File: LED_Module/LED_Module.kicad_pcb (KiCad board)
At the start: 2 copper layers, 46 parts, among them J1 Conn_02x05_Odd_Even, J2 Conn_01x03_Male, J3 ESP8266 Header, J4 Barrel_Jack, SW1 SW_Push, SW2 SW_Push, U1 LD1117S33TR_SOT223, U2 STM32F091RCTx, U3 TPS62A02DRL, U4 24AA32AF EEPROM

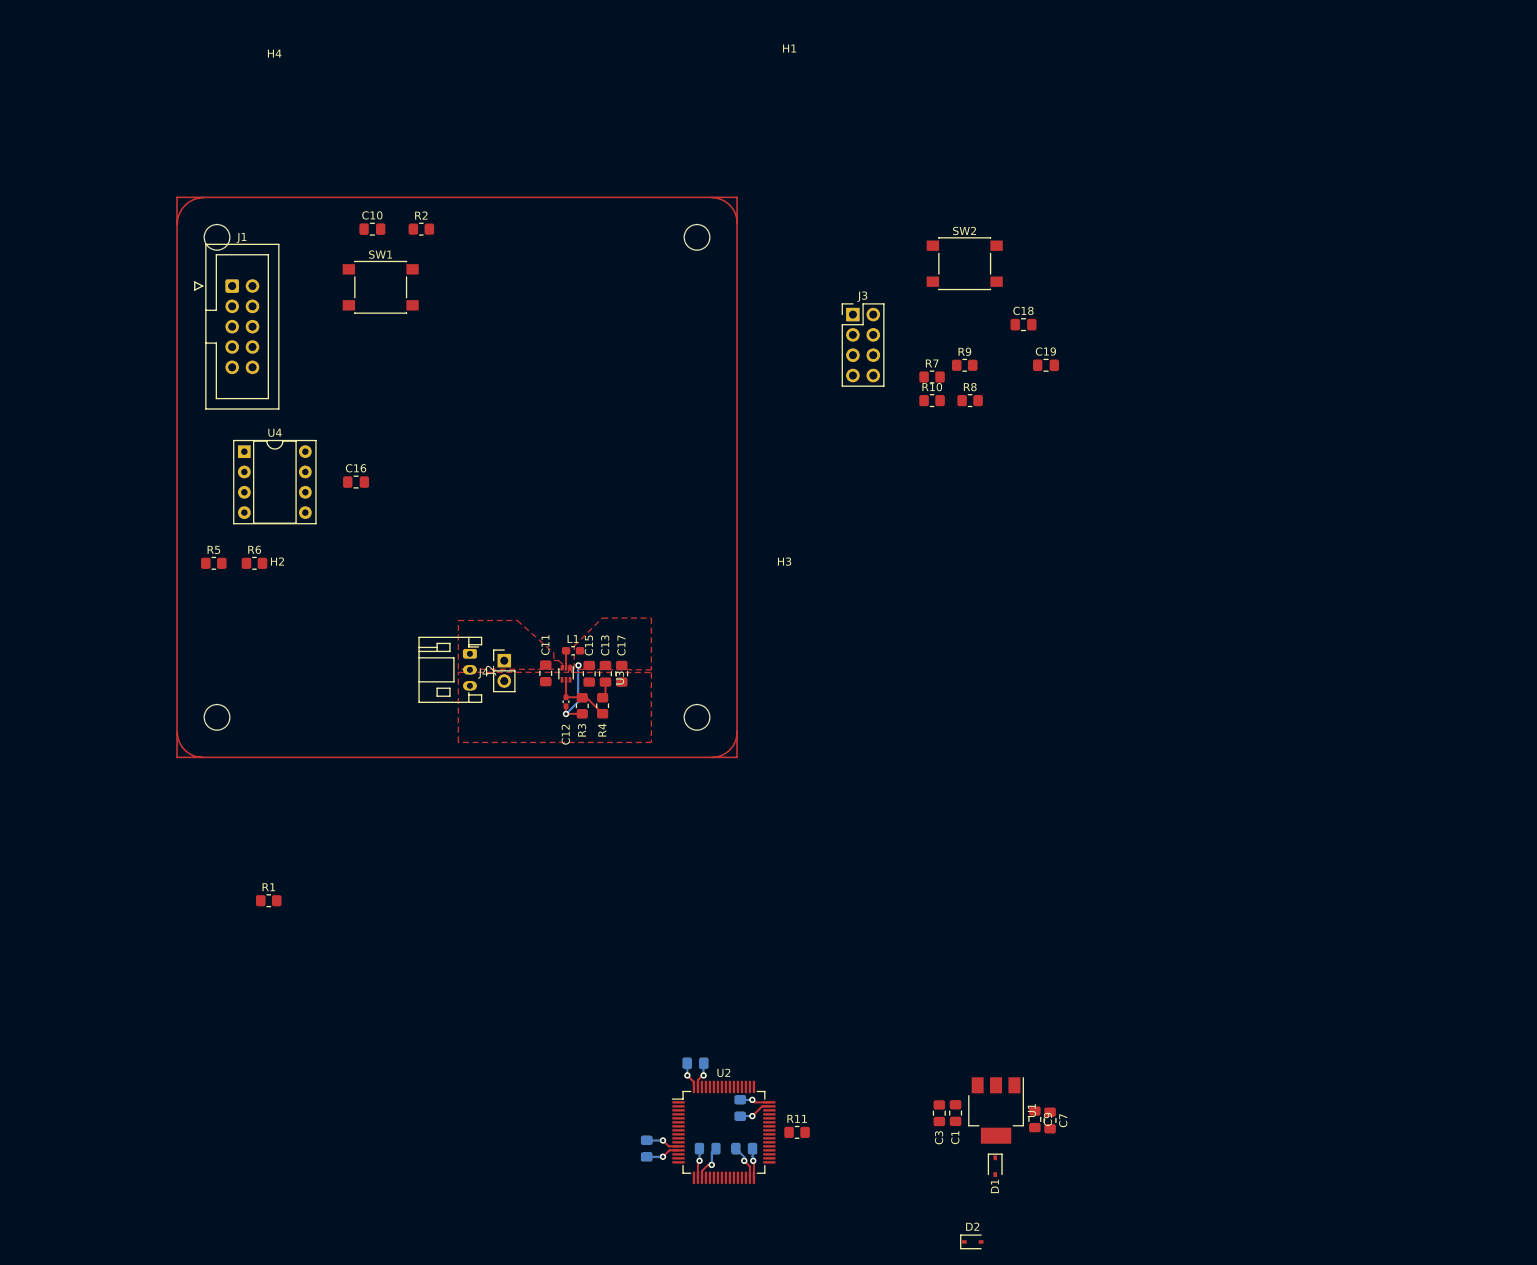
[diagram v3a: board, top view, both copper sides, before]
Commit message: Systems laid out and 3.3V connected
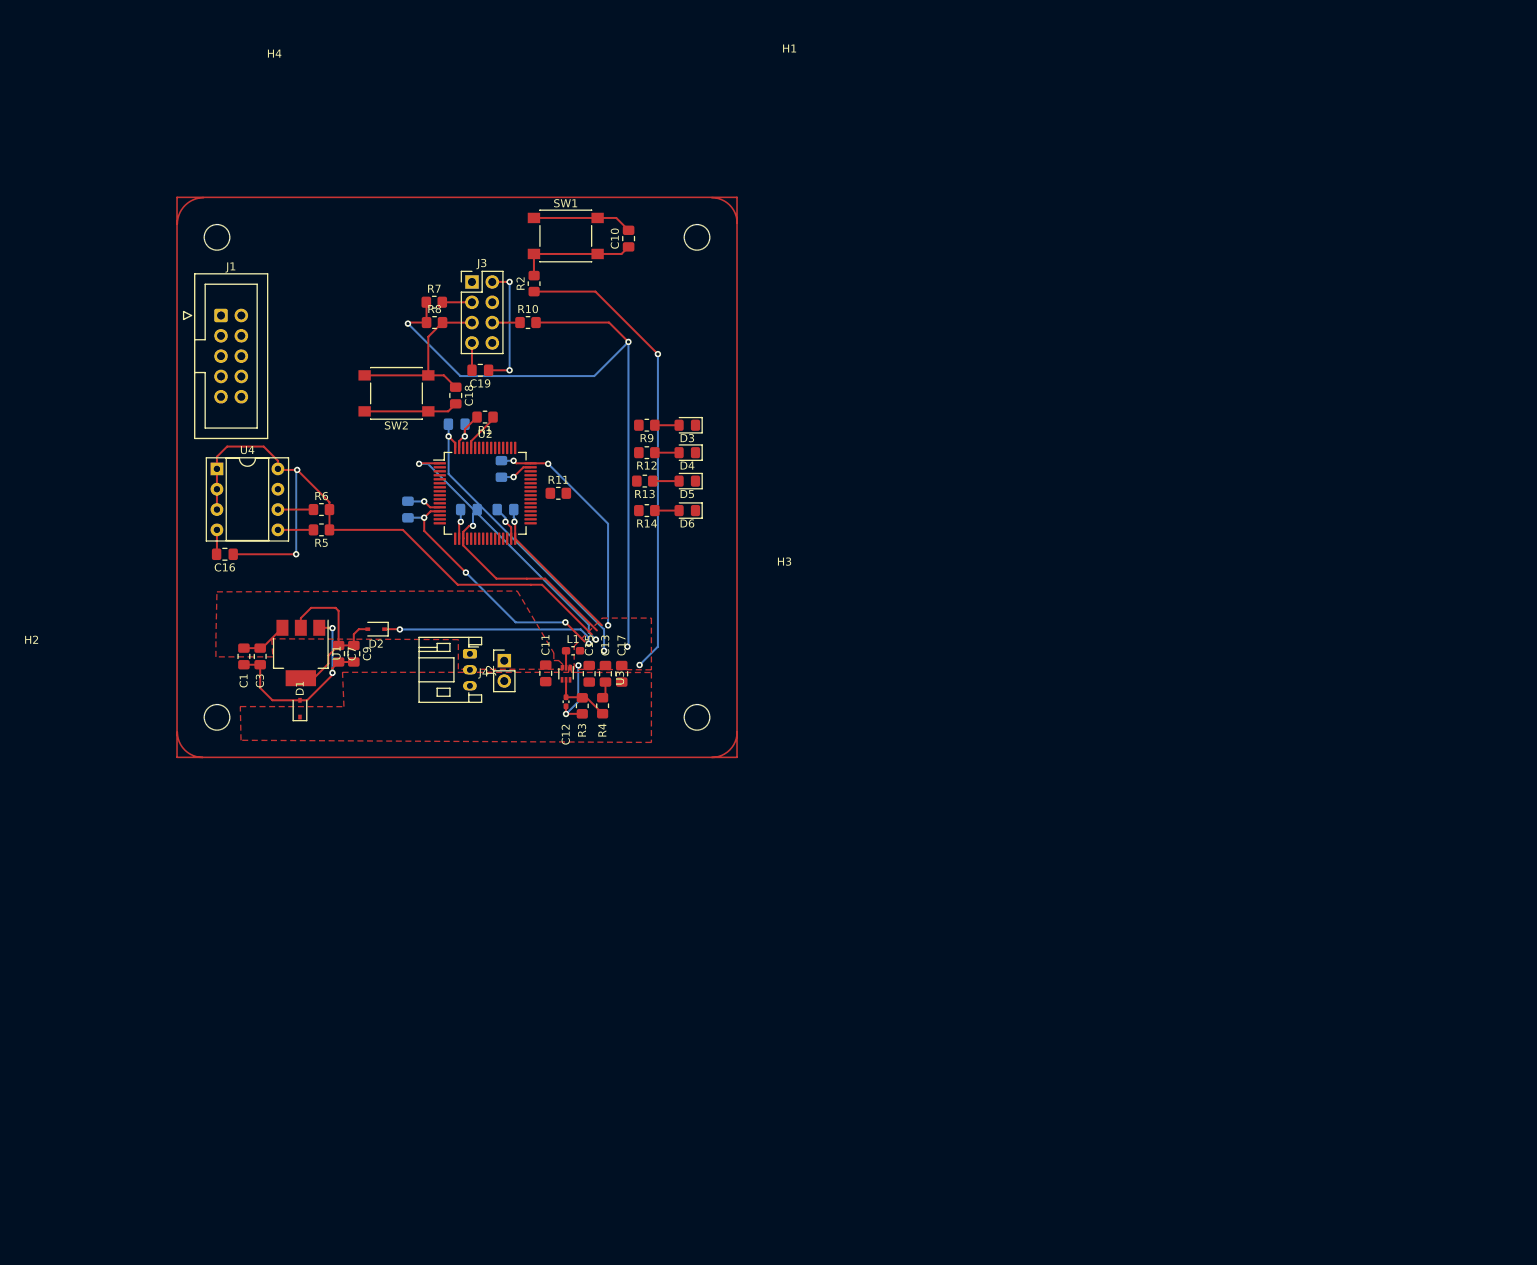
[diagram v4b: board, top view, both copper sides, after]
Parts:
- added D3: LED, LED_SMD:LED_0805_2012Metric_Pad1.15x1.40mm_HandSolder, F.Cu at (113.8, 78.5)
- added D4: LED, LED_SMD:LED_0805_2012Metric_Pad1.15x1.40mm_HandSolder, F.Cu at (113.8, 81.9)
- added D5: LED, LED_SMD:LED_0805_2012Metric_Pad1.15x1.40mm_HandSolder, F.Cu at (113.8, 85.5)
- added D6: LED, LED_SMD:LED_0805_2012Metric_Pad1.15x1.40mm_HandSolder, F.Cu at (113.8, 89.2)
- added R12: 3K, Resistor_SMD:R_0805_2012Metric_Pad1.20x1.40mm_HandSolder, F.Cu at (108.7, 81.9)
- added R13: 3K, Resistor_SMD:R_0805_2012Metric_Pad1.20x1.40mm_HandSolder, F.Cu at (108.5, 85.5)
- added R14: 3K, Resistor_SMD:R_0805_2012Metric_Pad1.20x1.40mm_HandSolder, F.Cu at (108.7, 89.2)
- R9: value R -> 3K
- moved D2 106.9 mm to (74.9, 104.0), turned to 180 degrees
- moved C7 106.4 mm to (70.2, 107.0)
- moved C1 105.7 mm to (58.4, 107.4)
- moved D1 104.0 mm to (65.4, 113.9), turned to 90 degrees
- moved U1 104.0 mm to (65.5, 107.0)
- moved C9 103.1 mm to (72.1, 107.0)
- moved C3 102.3 mm to (60.4, 107.4)
- moved C2 85.3 mm to (86.5, 89.0)
- moved C4 85.3 mm to (85.0, 78.4)
- moved C5 85.3 mm to (91.1, 89.0)
- moved C8 85.3 mm to (78.9, 89.0)
- moved C6 85.3 mm to (90.6, 83.9)
- moved R11 85.3 mm to (97.7, 87.0)
- moved U2 85.3 mm to (88.5, 87.0)
- moved SW2 72.9 mm to (77.4, 74.5), turned to 180 degrees
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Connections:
- D1 pad 1: GND -> BUCK_GND
- J3 pad 2: /CH_PD -> GND
- J3 pad 3: /RST -> /CH_PD
- J3 pad 4: 3.3V -> unconnected-(J3-Pad4)
- J3 pad 5: /PC12 -> /RST
- J3 pad 7: /GPIO2 -> 3.3V
- J3 pad 8: GND -> /PC12
- R9 pad 1: /GPIO2 -> Net-(D3-Pad2)
- R9 pad 2: GND -> /PC6
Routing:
- net 3.3V: track 29.5 -> 450.1 mm, vias 7 -> 23
- net GND: track 19.9 -> 66.1 mm, vias 5 -> 7
- net Net-(C1-Pad2): track 0.00 -> 27.1 mm, vias 0 -> 2
- net Net-(C7-Pad1): track 0.00 -> 23.3 mm
- net /RST: track 0.00 -> 23.0 mm
- net /NRST: track 0.00 -> 14.9 mm
- net 5V: track 0.06 -> 5.93 mm
- net /BOOT0: track 0.00 -> 4.98 mm
- net /EEPROM_SDA: track 0.00 -> 4.45 mm
- net /EEPROM_SCL: track 0.00 -> 4.45 mm
- net /CH_PD: track 0.00 -> 3.71 mm
- net /GPIO0: track 0.00 -> 3.47 mm
- net Net-(D5-Pad2): track 0.00 -> 3.28 mm
- net Net-(D6-Pad2): track 0.00 -> 3.03 mm
- net Net-(D4-Pad2): track 0.00 -> 3.03 mm
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
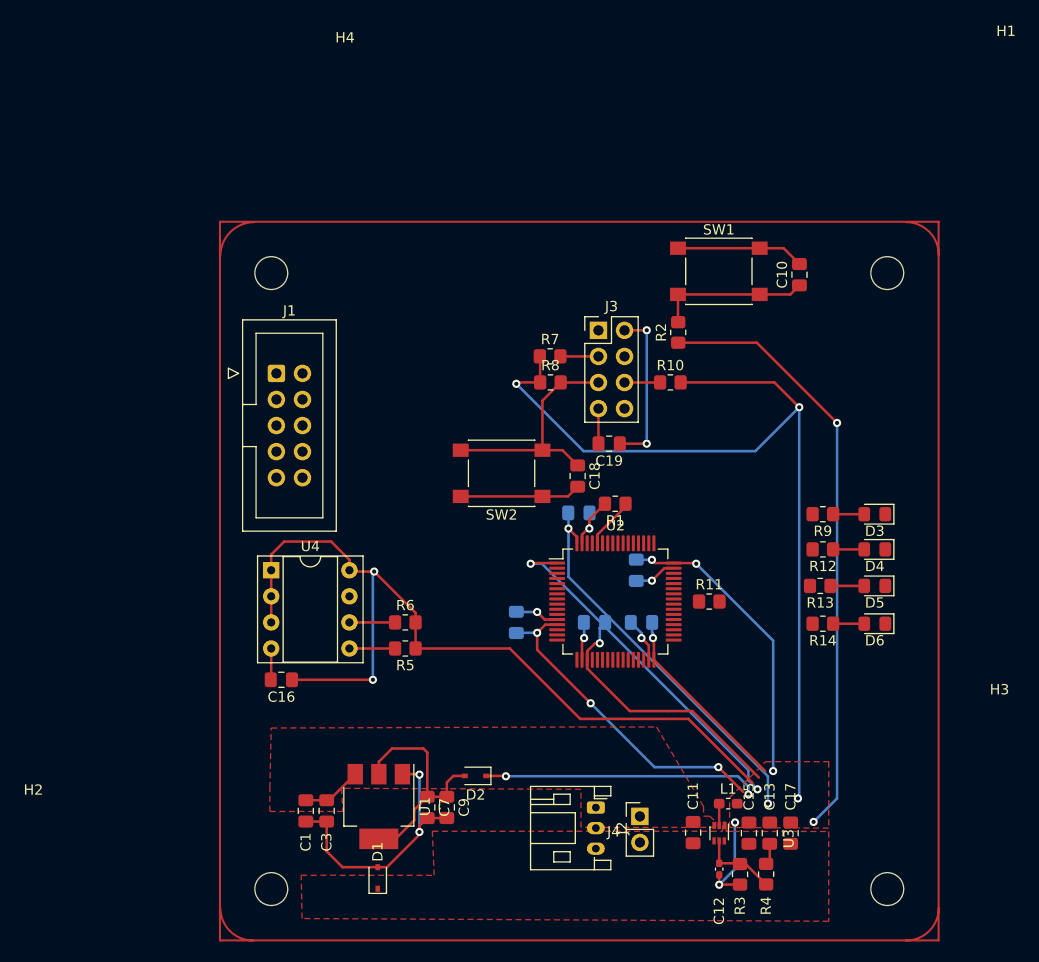
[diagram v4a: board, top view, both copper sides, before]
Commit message: Power and ground planes plus complete routing
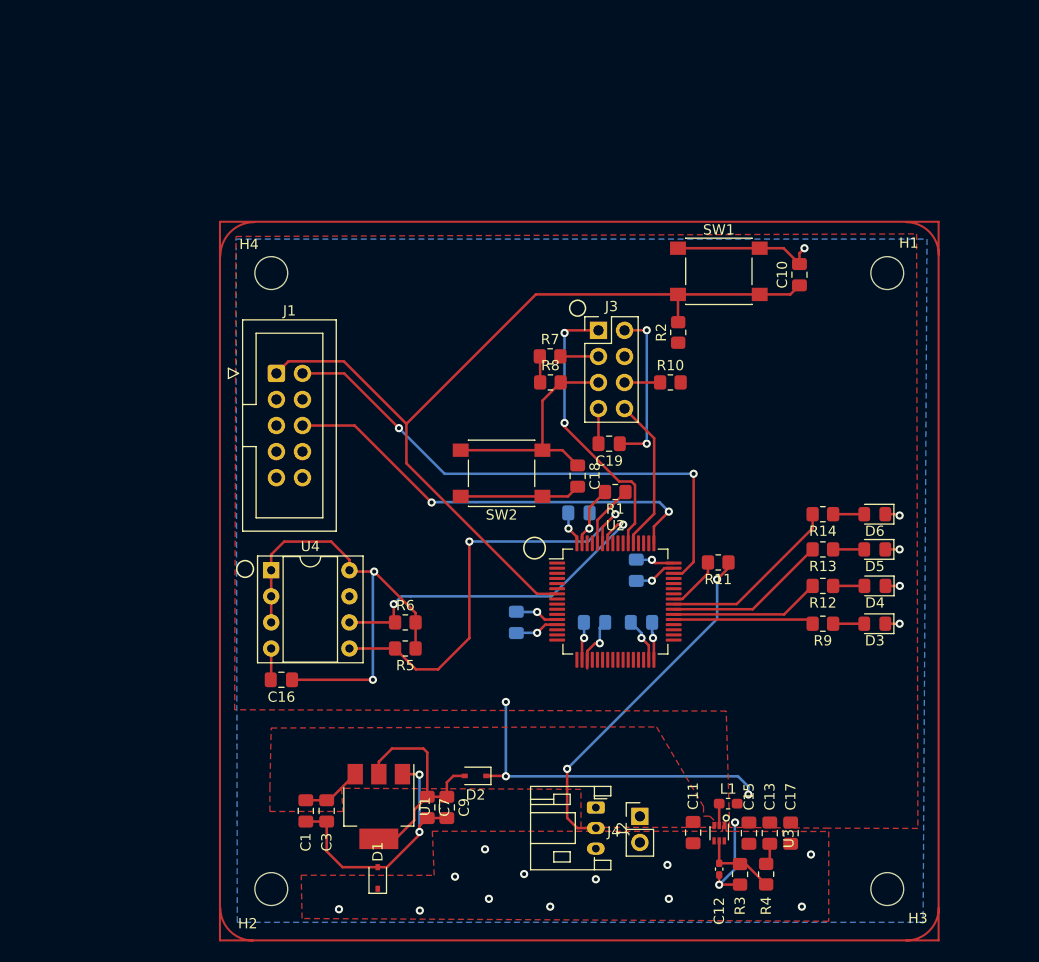
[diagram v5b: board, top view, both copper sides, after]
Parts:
- moved D3 10.7 mm to (113.8, 89.2)
- moved D6 10.7 mm to (113.8, 78.5)
- moved R14 10.7 mm to (108.7, 78.5)
- moved R9 10.7 mm to (108.7, 89.2)
- moved R11 3.91 mm to (98.5, 83.2), turned to 180 degrees
- moved R13 3.57 mm to (108.7, 81.9)
- moved D4 3.56 mm to (113.8, 85.5)
- moved D5 3.56 mm to (113.8, 81.9)
- moved R12 3.56 mm to (108.7, 85.5)
- moved R1 1.14 mm to (88.5, 76.3)
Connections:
- C10 pad 2: GND -> BUCK_GND
- C16 pad 2: GND -> BUCK_GND
- C18 pad 2: GND -> BUCK_GND
- C19 pad 1: GND -> BUCK_GND
- C2 pad 2: GND -> BUCK_GND
- C4 pad 2: GND -> BUCK_GND
- C5 pad 2: GND -> BUCK_GND
- C6 pad 2: GND -> BUCK_GND
- C8 pad 2: GND -> BUCK_GND
- D3 pad 1: GND -> BUCK_GND
- D4 pad 1: GND -> BUCK_GND
- D5 pad 1: GND -> BUCK_GND
- D6 pad 1: GND -> BUCK_GND
- J1 pad 3: GND -> BUCK_GND
- J1 pad 4: GND -> BUCK_GND
- J3 pad 2: GND -> BUCK_GND
- R1 pad 2: GND -> BUCK_GND
- SW1 pad 1: GND -> BUCK_GND
- SW2 pad 1: GND -> BUCK_GND
- U2 pad 12: GND -> BUCK_GND
- U2 pad 18: GND -> BUCK_GND
- U2 pad 31: GND -> BUCK_GND
- U2 pad 47: GND -> BUCK_GND
- U2 pad 63: GND -> BUCK_GND
- U4 pad 4: GND -> BUCK_GND
- U4 pad 7: GND -> BUCK_GND
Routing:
- net 3.3V: track 450.1 -> 116.9 mm, vias 23 -> 12
- net BUCK_GND: track 2.10 -> 76.7 mm, vias 0 -> 24
- net /NRST: track 14.9 -> 86.1 mm
- net GND: track 66.1 -> 0.00 mm, vias 7 -> 0
- net /PA13: track 0.00 -> 53.1 mm, vias 0 -> 2
- net /PA14: track 0.00 -> 42.9 mm, vias 0 -> 2
- net /EEPROM_SDA: track 4.45 -> 41.9 mm, vias 0 -> 2
- net Net-(J2-Pad2): track 0.00 -> 34.6 mm, vias 0 -> 2
- net /EEPROM_SCL: track 4.45 -> 34.6 mm, vias 0 -> 2
- net /PD2: track 0.00 -> 27.7 mm, vias 0 -> 2
- net /PC9: track 0.00 -> 18.0 mm
- net /PC8: track 0.00 -> 15.9 mm
- net /PC12: track 0.00 -> 15.2 mm
- net /PC7: track 0.00 -> 14.7 mm
- net /PC6: track 0.00 -> 13.7 mm
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- added copper zone on B.Cu, net BUCK_GND

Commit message: Added bulk capacitor, diode, and some extra vias
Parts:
- added C14: 100uF, Capacitor_THT:C_Rect_L7.0mm_W2.0mm_P5.00mm, F.Cu at (89.9, 111.6)
- added D7: BAT60JFILM, Diode_SMD:D_SOD-323, F.Cu at (109.6, 106.0)
- moved J4 2.18 mm to (93.1, 108.0)
- moved L1 0.39 mm to (99.6, 107.1)
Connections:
- C12 pad 1: 3.3V -> BUCK_3.3V
- C13 pad 1: 3.3V -> BUCK_3.3V
- C15 pad 1: 3.3V -> BUCK_3.3V
- C17 pad 1: 3.3V -> BUCK_3.3V
- L1 pad 2: 3.3V -> BUCK_3.3V
- R3 pad 1: 3.3V -> BUCK_3.3V
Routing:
- net 3.3V: track 116.9 -> 82.3 mm, vias 12 -> 9
- net BUCK_3.3V: track 0.00 -> 9.71 mm, vias 0 -> 2
- net BUCK_GND: track 76.7 -> 85.0 mm, vias 24 -> 25
- net /PB11: track 0.00 -> 4.50 mm, vias 0 -> 1
- net /PB14: track 0.00 -> 4.24 mm, vias 0 -> 1
- net /PB10: track 0.00 -> 3.70 mm, vias 0 -> 1
- net /PB13: track 0.00 -> 3.64 mm, vias 0 -> 1
- net /PA3: track 0.00 -> 3.55 mm, vias 0 -> 1
- net /PA6: track 0.00 -> 3.10 mm, vias 0 -> 1
- net /PA5: track 0.00 -> 2.94 mm, vias 0 -> 1
- net /PA2: track 0.00 -> 2.36 mm, vias 0 -> 1
- net Net-(L1-Pad1): track 1.93 -> 0.00 mm
- added copper zone on F.Cu, net BUCK_3.3V

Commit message: PCB design updated for week 8 design review
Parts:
- added D8: LED, LED_SMD:LED_0805_2012Metric_Pad1.15x1.40mm_HandSolder, F.Cu at (57.5, 101.0)
- added D9: LED, LED_SMD:LED_0805_2012Metric_Pad1.15x1.40mm_HandSolder, F.Cu at (116.6, 101.6)
- added R15: 3K, Resistor_SMD:R_0805_2012Metric_Pad1.20x1.40mm_HandSolder, F.Cu at (62.2, 100.8)
- added R16: 3K, Resistor_SMD:R_0805_2012Metric_Pad1.20x1.40mm_HandSolder, F.Cu at (116.6, 106.4)
- C13, C15, C17: footprint Capacitor_SMD:C_0805_2012Metric_Pad1.18x1.45mm_HandSolder -> Capacitor_SMD:C_1206_3216Metric_Pad1.33x1.80mm_HandSolder
- moved C17 1.66 mm to (107.2, 109.1)
- moved C13 1.41 mm to (104.9, 109.1)
- moved C15 1.17 mm to (102.6, 109.1)
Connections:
- net BUCK_GND renamed GND
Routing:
- net 3.3V: track 82.3 -> 35.9 mm, vias 9 -> 7
- net GND: track 85.0 -> 87.8 mm, vias 25 -> 27
- net Net-(D8-Pad2): track 0.00 -> 2.78 mm
- net Net-(D9-Pad2): track 0.00 -> 2.74 mm
- net Net-(L1-Pad1): track 0.00 -> 1.78 mm
- net 5V: track 5.93 -> 7.43 mm
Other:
- board outline added: 70 x 70 mm

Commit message: Final PCB Design used in order from PCB Way
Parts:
- C14: footprint Capacitor_THT:C_Rect_L7.0mm_W2.0mm_P5.00mm -> Capacitor_THT:C_Radial_D10.0mm_H16.0mm_P5.00mm
- moved J2 13.1 mm to (73.5, 106.9), turned to 0 degrees
- moved C10 12.2 mm to (94.3, 55.0)
- moved SW1 12.2 mm to (86.4, 54.7)
- moved C14 4.57 mm to (85.4, 112.1)
- moved U1 2.74 mm to (62.8, 106.4)
- moved C1 2.57 mm to (55.9, 106.8)
- moved C3 2.57 mm to (57.9, 106.8)
- moved C7 2.50 mm to (67.8, 106.4)
- moved C9 2.23 mm to (70.0, 106.4)
- moved D2 1.88 mm to (73.1, 103.4)
- moved D1 1.88 mm to (63.6, 113.4)
- moved D8 1.88 mm to (55.7, 100.4)
- moved R15 1.88 mm to (60.4, 100.3)
- moved D7 1.07 mm to (109.6, 105.0)
- moved C17 0.20 mm to (107.4, 109.1)
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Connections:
- J1 pad 10: /U5V -> unconnected-(J1-Pad10)
- J1 pad 7: /V3.3_IN -> unconnected-(J1-Pad7)
- J1 pad 8: /V3.3_IN -> unconnected-(J1-Pad8)
- J1 pad 9: /U5V -> unconnected-(J1-Pad9)
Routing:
- net /NRST: track 86.1 -> 75.1 mm
- net 5V: track 7.43 -> 3.77 mm
- net 3.3V: track 35.9 -> 33.0 mm
- net Net-(J2-Pad2): track 34.6 -> 37.4 mm
- net Net-(C1-Pad2): track 27.1 -> 28.3 mm
- net Net-(C7-Pad1): track 23.3 -> 23.9 mm
- net GND: track 87.8 -> 87.3 mm
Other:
- board text added: "ECE 477 Team 5 Spring 23 BoxFish Zack Breisch Jonathon Snyder Luke Diehm Agrim Bharat"
